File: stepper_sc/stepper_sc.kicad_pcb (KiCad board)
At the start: 2 copper layers, 90 x 120 mm, 24 parts, among them J1 PWR_24V, J10 BUZZ, J11 Black_Pill_front, J12 Black_Pill_back, J2 PUL, J3 DIR, J4 ES_L, J5 ES_R, J6 JOGL, J7 JOGR, J8 STEPL, J9 STEPR, Q1 BC547, Q2 BC547, U1 78M05

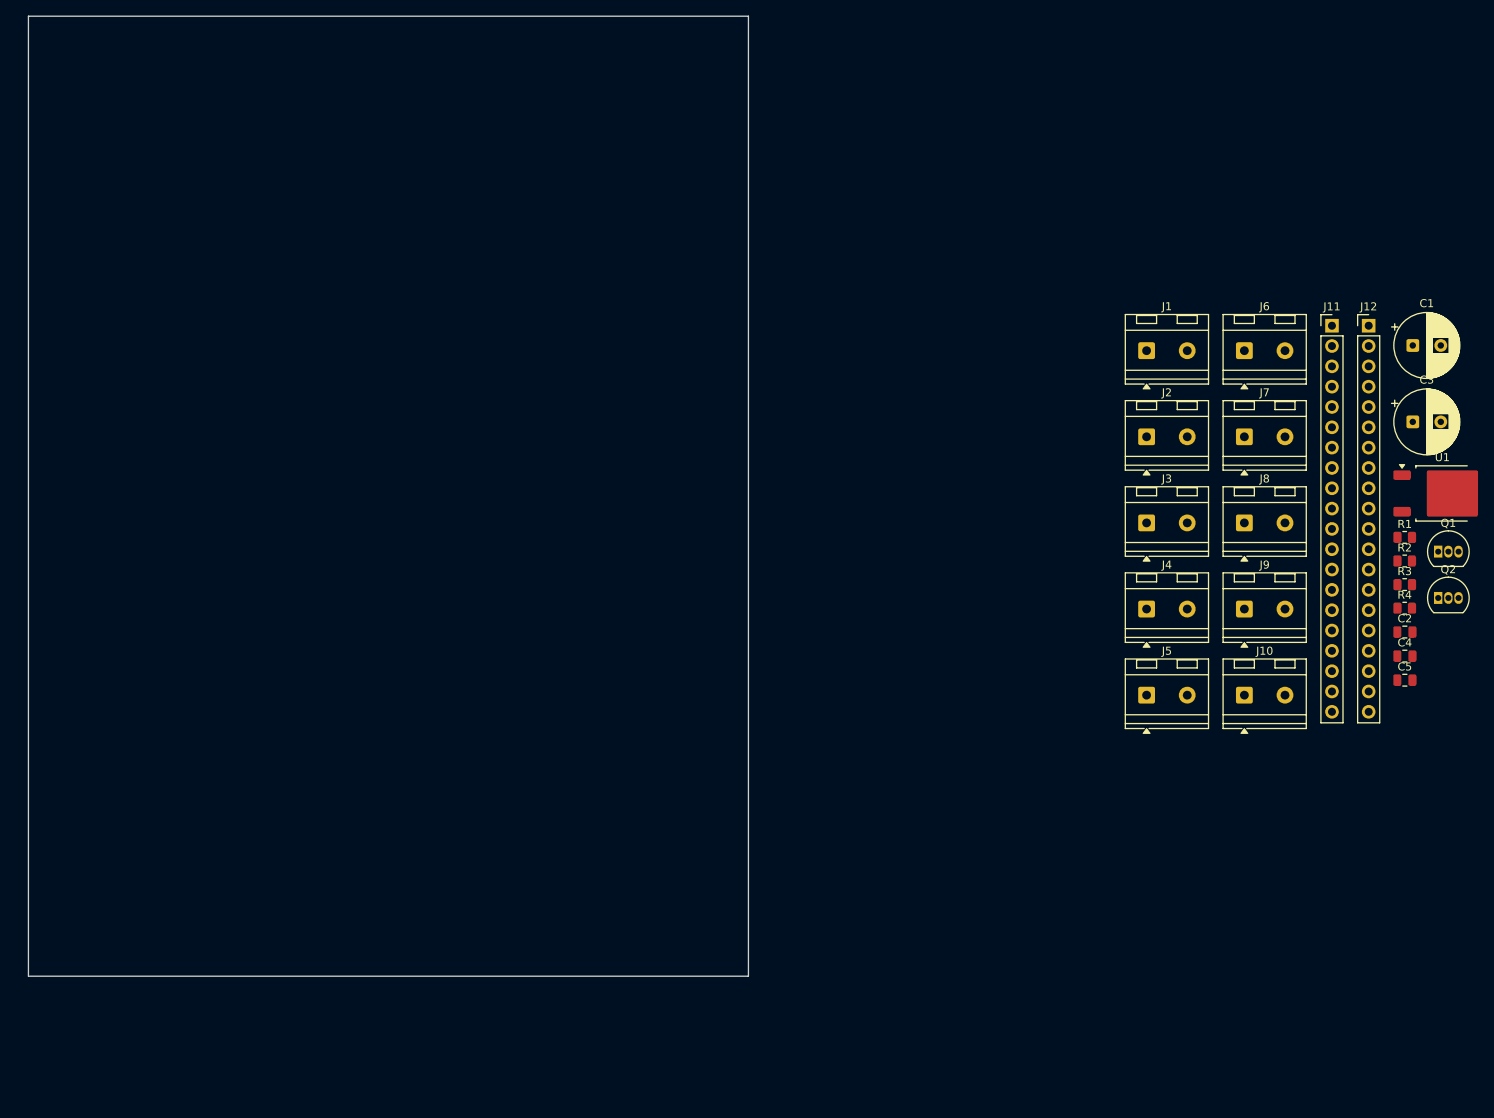
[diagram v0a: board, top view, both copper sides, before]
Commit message: Fix Q1/Q2 net assignments + orbit duplicate bug
- stepper_sc.kicad_pcb: assign correct nets to Q1 and Q2 pads
  BC547 TO-92_Inline pinout: pad1=C, pad2=B, pad3=E
  Q1: C→Net-(J2-Pin_2), B→Net-(Q1-PadB), E→GND
  Q2: C→Net-(J3-Pin_2), B→Net-(Q2-PadB), E→GND
  Root cause: KiCad couldn't map Q_NPN symbolic pins (B,C,E) to
  numeric pads (1,2,3) during Update PCB from Schematic.

- demo_orbit_all.py: fix duplicate footprint bug
  Use update_items(fp) without begin_commit/push_commit wrapper.
  Having both caused each fp to be sent twice → 1325 duplicates.

Co-Authored-By: Claude Sonnet 4.6 <noreply@anthropic.com>
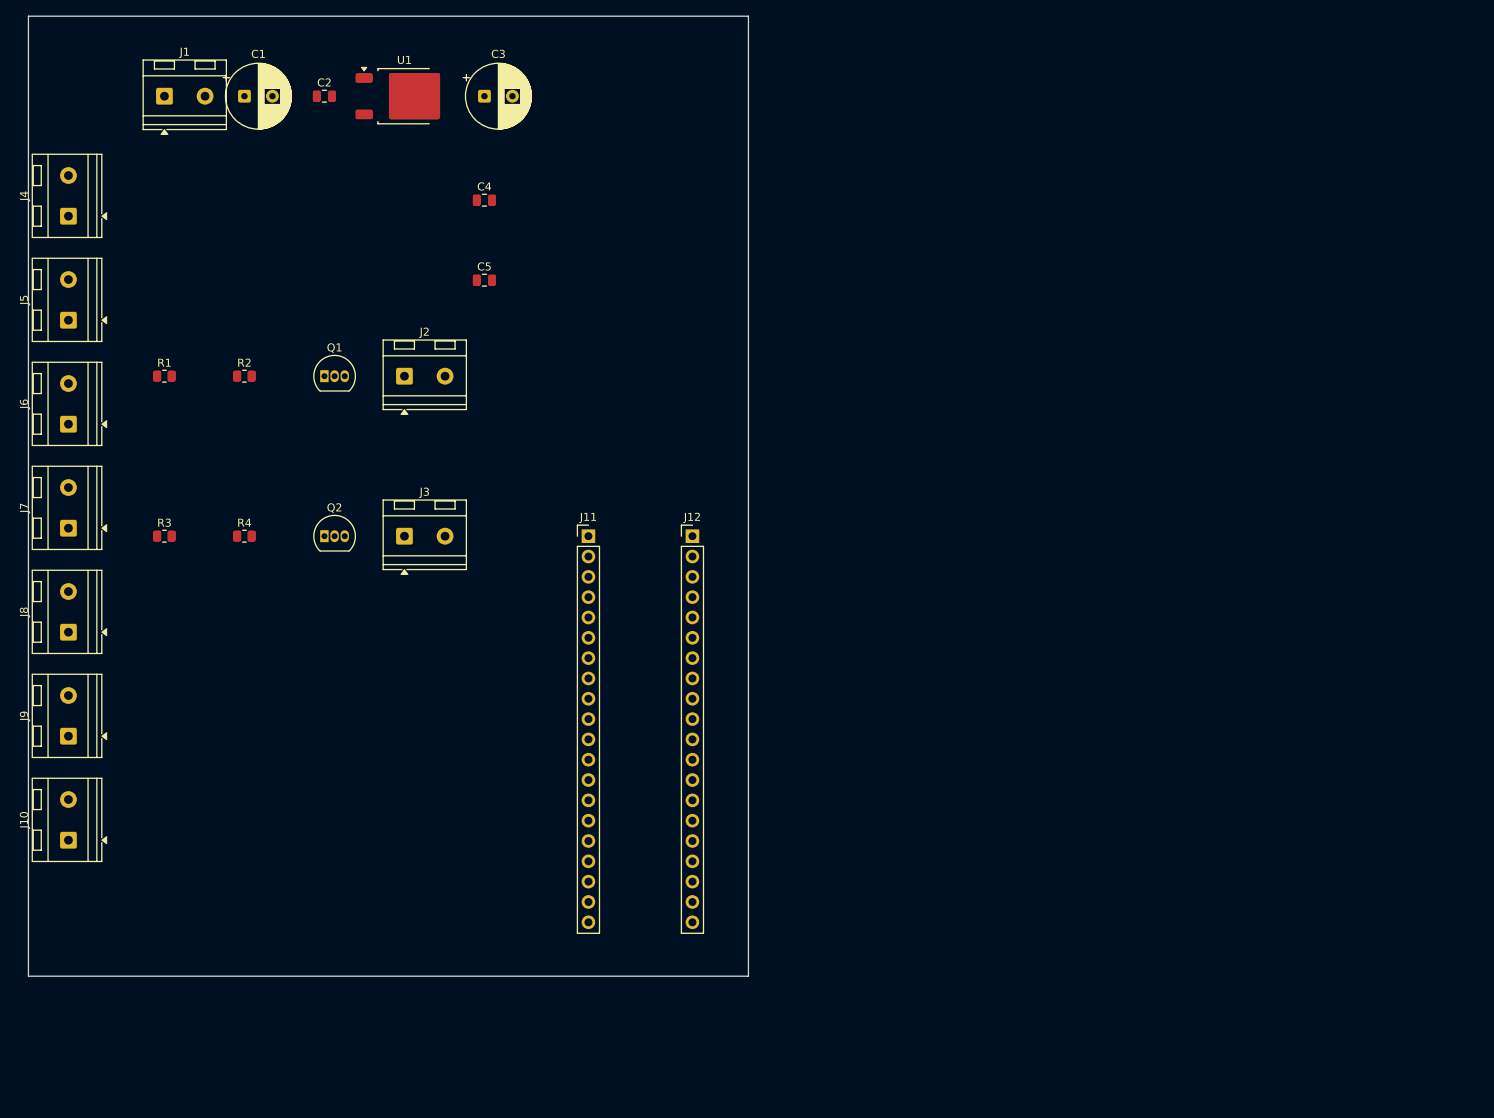
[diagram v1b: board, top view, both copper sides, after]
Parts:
- moved R1 156.3 mm to (42.0, 70.0)
- moved R3 155.1 mm to (42.0, 90.0)
- moved C2 150.7 mm to (62.0, 35.0)
- moved C1 149.3 mm to (52.0, 35.0)
- moved J10 148.1 mm to (30.0, 128.0), turned to 90 degrees
- moved J9 147.8 mm to (30.0, 115.0), turned to 90 degrees
- moved J8 147.6 mm to (30.0, 102.0), turned to 90 degrees
- moved J7 147.4 mm to (30.0, 89.0), turned to 90 degrees
- moved J6 147.3 mm to (30.0, 76.0), turned to 90 degrees
- moved R2 146.9 mm to (52.0, 70.0)
- moved R4 145.3 mm to (52.0, 90.0)
- moved J4 143.4 mm to (30.0, 50.0), turned to 90 degrees
- moved J5 142.7 mm to (30.0, 63.0), turned to 90 degrees
- moved Q1 140.9 mm to (62.0, 70.0)
- moved Q2 139.4 mm to (62.0, 90.0)
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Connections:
- Q1 pad 1: (no net) -> Net-(J2-Pin_2)
- Q1 pad 2: (no net) -> Net-(Q1-PadB)
- Q1 pad 3: (no net) -> GND
- Q2 pad 1: (no net) -> Net-(J3-Pin_2)
- Q2 pad 2: (no net) -> Net-(Q2-PadB)
- Q2 pad 3: (no net) -> GND

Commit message: PCB: swap C1/C3→CP_Elec_8x6.2 SMD, Q1/Q2→SOT-23 SMD; assign pad nets
- C1, C3: Capacitor_THT:CP_Radial_D8.0mm_P3.50mm → Capacitor_SMD:CP_Elec_8x6.2
- Q1, Q2: Package_TO_SOT_THT:TO-92_Inline → Package_TO_SOT_SMD:SOT-23
- Q1 pads: pad1(B)→Net-(Q1-PadB), pad2(E)→GND, pad3(C)→Net-(J2-Pin_2)
- Q2 pads: pad1(B)→Net-(Q2-PadB), pad2(E)→GND, pad3(C)→Net-(J3-Pin_2)
- Re-placed all 24 footprints after footprint swap

Co-Authored-By: Claude Sonnet 4.6 <noreply@anthropic.com>
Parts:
- C1, C3: footprint Capacitor_THT:CP_Radial_D8.0mm_P3.50mm -> Capacitor_SMD:CP_Elec_8x6.2
- Q1, Q2: footprint Package_TO_SOT_THT:TO-92_Inline -> Package_TO_SOT_SMD:SOT-23
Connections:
- Q1 pad 1: Net-(J2-Pin_2) -> Net-(Q1-PadB)
- Q1 pad 2: Net-(Q1-PadB) -> GND
- Q1 pad 3: GND -> Net-(J2-Pin_2)
- Q2 pad 1: Net-(J3-Pin_2) -> Net-(Q2-PadB)
- Q2 pad 2: Net-(Q2-PadB) -> GND
- Q2 pad 3: GND -> Net-(J3-Pin_2)

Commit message: PCB: reorganize terminal block column, extend board outline
- Move J1 above J4 in the left screw terminal column (rot=90°, 13mm spacing)
- Move J2, J3 into the same column below J10 (y=141, y=154, rot=90°)
- Extend edge cuts to fit full terminal column (J1→J2→J3→J4→...→J10)
- Board outline: x=25→115, y=25.26→160.66 (4.00mm gap above J1 and below J3 body)

Co-Authored-By: Claude Sonnet 4.6 <noreply@anthropic.com>
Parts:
- moved J2 82.5 mm to (30.0, 141.0), turned to 90 degrees
- moved J3 76.6 mm to (30.0, 154.0), turned to 90 degrees
- moved J1 12.2 mm to (30.0, 37.0), turned to 90 degrees
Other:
- board size 90 x 120 mm -> 90 x 135.4 mm

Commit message: PCB: layout power rail row — caps, regulator, equal spacing
- J1 placed in terminal column above J4, rot=90°, 13mm spacing
- J2, J3 moved into terminal column below J10 (y=141, y=154)
- Edge cuts extended and fine-tuned: 4.00mm gap above J1 and below J3 bodies
- C1 rotated +90° to match J1 polarity (+24V at bottom, GND at top)
- C2, C3, C4 rotated +90° to match polarity consistently
- C4 moved from (82,48) to power rail row at y=35
- U1 rotated 90° (3× -90°), center aligned to y=35
- Equal body spacing (4.13mm gaps) between C1–C2–U1–C3–C4

Co-Authored-By: Claude Sonnet 4.6 <noreply@anthropic.com>
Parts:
- moved C4 16.4 mm to (92.0, 35.0), turned to 90 degrees
- moved U1 1.71 mm to (70.3, 35.0), turned to 90 degrees
- moved C2 0.44 mm to (61.6, 35.0), turned to 90 degrees
- moved C3 0.44 mm to (82.4, 35.0), turned to 90 degrees
- turned C1 to 90 degrees

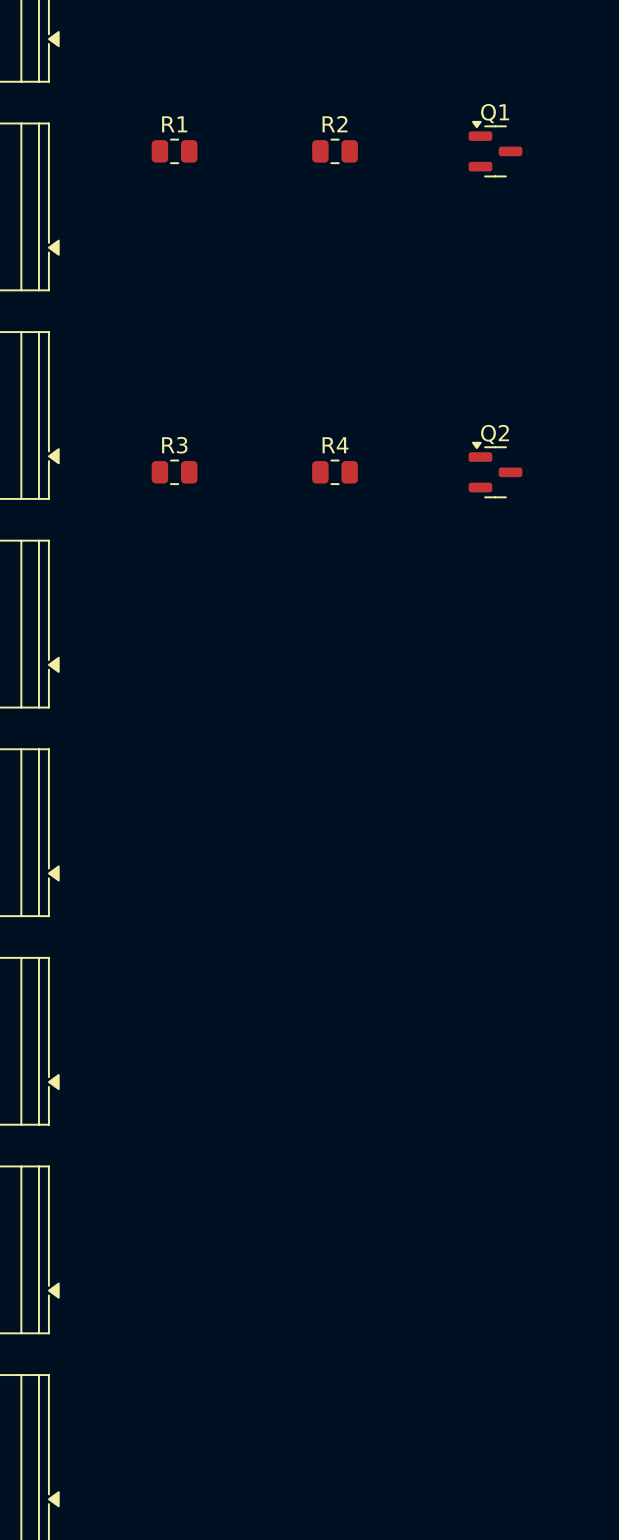
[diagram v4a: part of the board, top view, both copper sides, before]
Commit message: PCB: place NPN buffer groups Q1/Q2 aligned to screw terminals
- Q1 group (Q1 rot=0°, R2 rot=-90°, R1 rot=90°) at y=135.92
  Q1 pad3 (collector) aligned with J2 pad2 — direct horizontal trace
- Q2 group (Q2 rot=0°, R4 rot=-90°, R3 rot=90°) at y=148.92
  Q2 pad3 (collector) aligned with J3 pad2 — direct horizontal trace
- Both groups 2mm right of terminal block edge, equal body spacing

Co-Authored-By: Claude Sonnet 4.6 <noreply@anthropic.com>
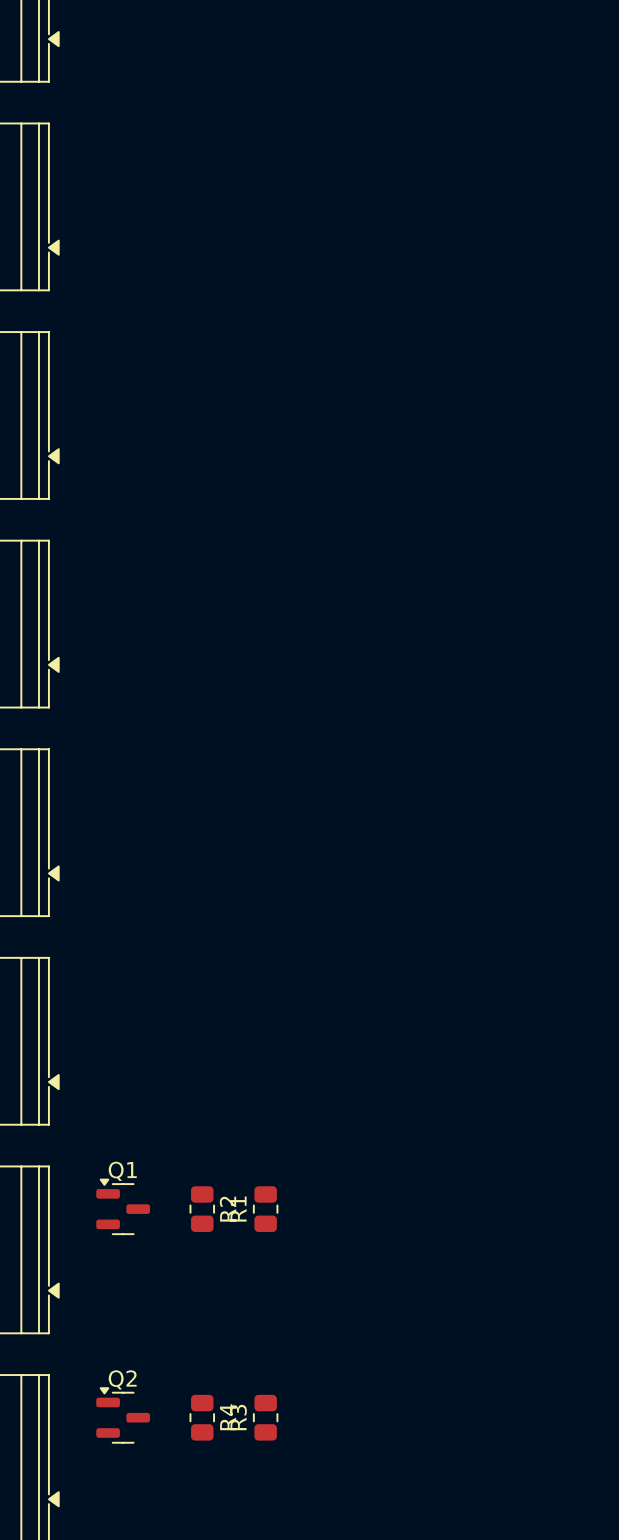
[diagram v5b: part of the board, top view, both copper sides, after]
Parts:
- moved Q1 69.9 mm to (38.8, 135.9)
- moved R2 66.4 mm to (43.7, 135.9), turned to -90 degrees
- moved R1 66.2 mm to (47.7, 135.9), turned to 90 degrees
- moved Q2 63.3 mm to (38.8, 148.9)
- moved R4 59.5 mm to (43.7, 148.9), turned to -90 degrees
- moved R3 59.2 mm to (47.7, 148.9), turned to 90 degrees

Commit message: PCB: align C5 +5V pad with J12 pin20, shift J11/J12/C5 group +10mm right
- C5 pad1 (+5V) x-aligned with J12 pin20 (+5V) at x=95.26mm
- J11/J12/C5 group shifted +10mm right (J11/J12 pin1 now at x=47)
- Add align_c5_j12.py helper script

Co-Authored-By: Claude Sonnet 4.6 <noreply@anthropic.com>
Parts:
- moved J12 72.9 mm to (47.0, 50.0), turned to 90 degrees
- moved J11 55.1 mm to (47.0, 63.0), turned to 90 degrees
- moved C5 12.4 mm to (94.3, 56.5), turned to 180 degrees

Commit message: PCB: add GND copper pour on F.Cu and B.Cu via IPC
- gnd_pour.py: creates filled Zone on both layers, net=GND
- Zone outline 0.5mm inset from Edge.Cuts (25.5,25.5)..(114.5,160.5)
- Zones refilled automatically after creation

Co-Authored-By: Claude Sonnet 4.6 <noreply@anthropic.com>
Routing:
- added copper zone on B.Cu, net GND
- added copper zone on F.Cu, net GND
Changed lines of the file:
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@@
 		(layer "Edge.Cuts")
+	)
+	(zone
+		(net 1)
+		(net_name "GND")
+		(layer "F.Cu")
+		(hatch edge 0.5)
+		(connect_pads
+			(clearance 0.3)
+		)
+		(min_thickness 0.25)
+		(filled_areas_thickness no)
+		(fill yes
+			(thermal_gap 0)
+			(thermal_bridge_width 0)
+		)
+		(polygon
+			(pts
+				(xy 25.5 25.5) (xy 114.5 25.5) (xy 114.5 160.5) (xy 25.5 160.5)
+			)
+		)
+	)
+	(zone
+		(net 1)
+		(net_name "GND")
+		(layer "B.Cu")
+		(hatch edge 0.5)
+		(connect_pads
+			(clearance 0.3)
+		)
+		(min_thickness 0.25)
+		(filled_areas_thickness no)
+		(fill yes
+			(thermal_gap 0)
+			(thermal_bridge_width 0)
+		)
+		(polygon
+			(pts
+				(xy 25.5 25.5) (xy 114.5 25.5) (xy 114.5 160.5) (xy 25.5 160.5)
+			)
+		)
 	)
 	(embedded_fonts no)

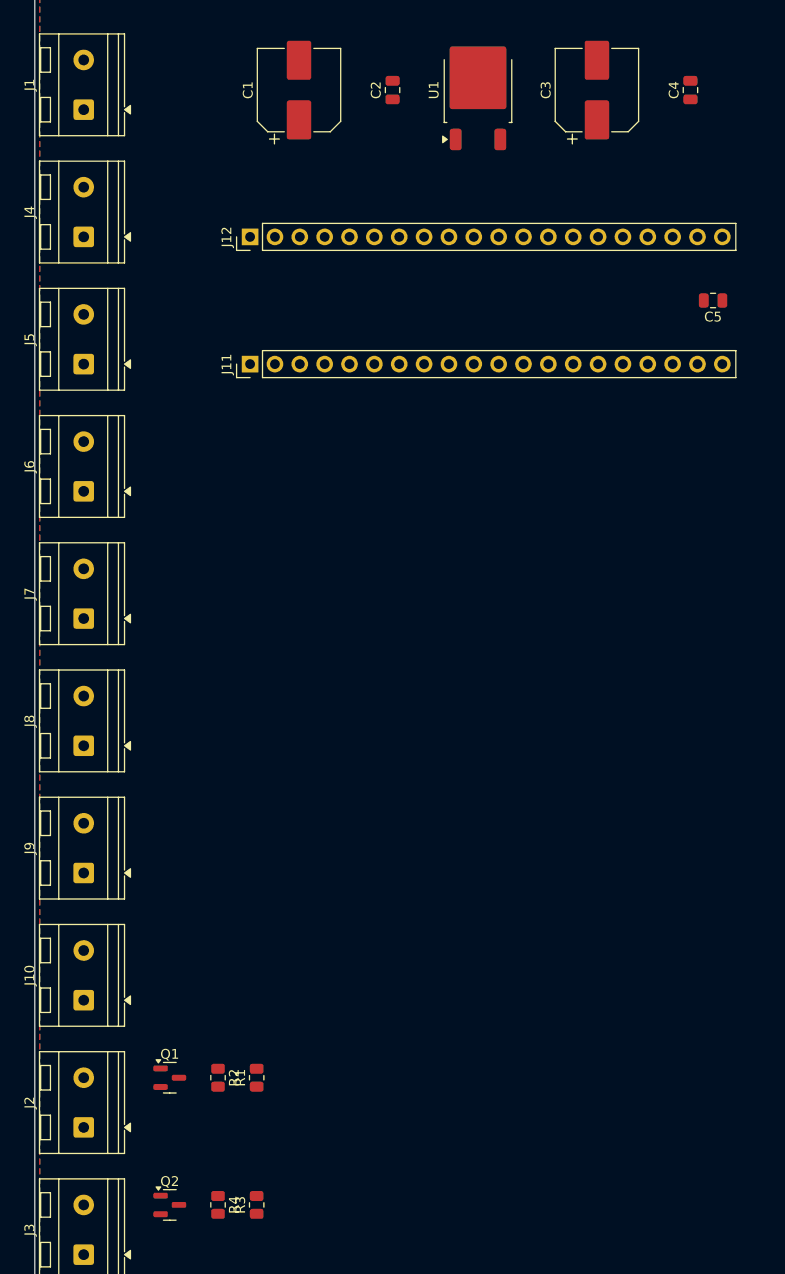
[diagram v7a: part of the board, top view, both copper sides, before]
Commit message: router: first homegrown A* PCB autorouter
- router/grid.py: two-layer obstacle grid (F.Cu + B.Cu), 0.1mm resolution
- router/astar.py: A* pathfinder, 8-directional + via transitions
- router/segments.py: convert A* path to 45° track segments
- router/router.py: main entry point, queries KiCad IPC, routes all unconnected nets

First run: 9 nets routed, 124 tracks + 4 vias, 0 failures.
No crossings — per-net pad exclusion prevents short circuits.

Co-Authored-By: Claude Sonnet 4.6 <noreply@anthropic.com>
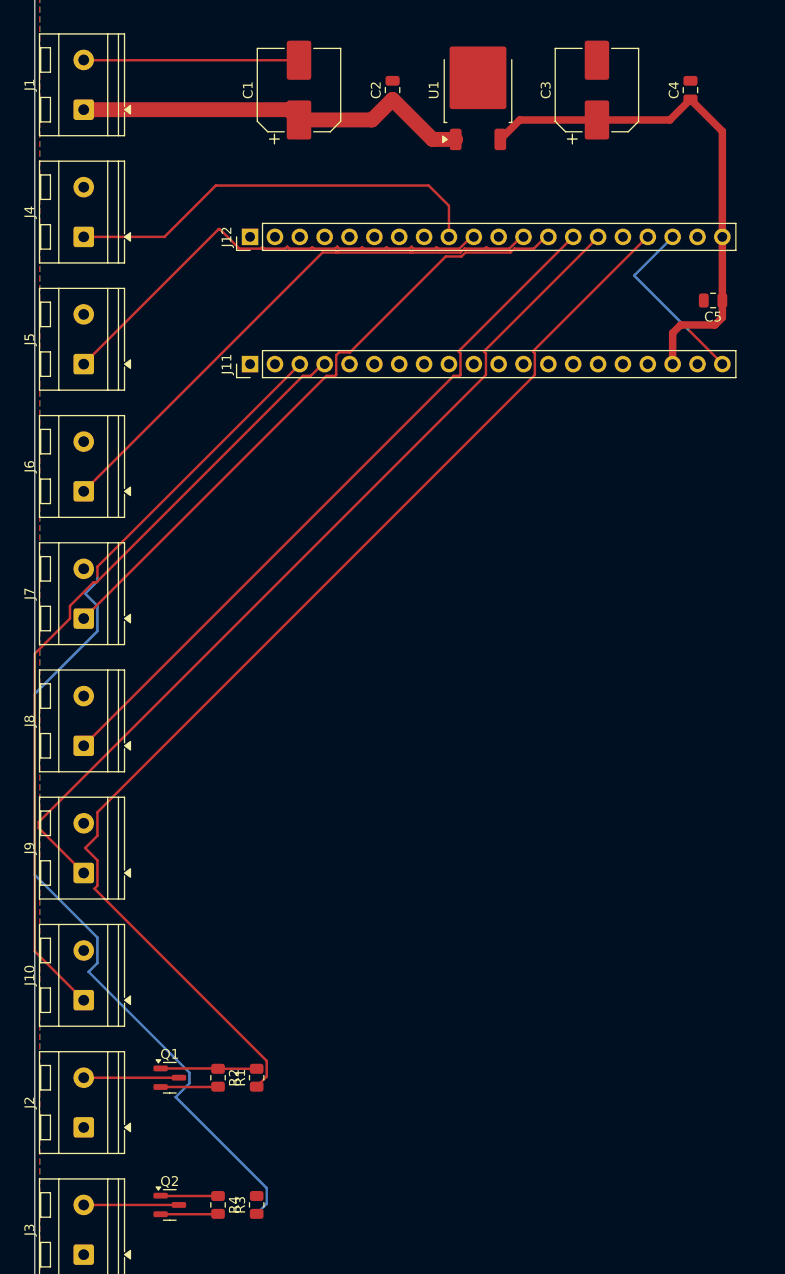
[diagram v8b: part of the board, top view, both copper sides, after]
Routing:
- net Net-(J12-Pin_17): track 0.00 -> 119.1 mm
- net Net-(J11-Pin_3): track 0.00 -> 111.2 mm, vias 0 -> 2
- net Net-(J12-Pin_15): track 0.00 -> 90.8 mm
- net Net-(J10-Pin_1): track 0.00 -> 80.2 mm
- net Net-(J12-Pin_14): track 0.00 -> 73.2 mm
- net Net-(J12-Pin_13): track 0.00 -> 64.9 mm
- net Net-(J12-Pin_12): track 0.00 -> 56.0 mm
- net +5V: track 0.00 -> 53.7 mm
- net Net-(J12-Pin_10): track 0.00 -> 47.9 mm
- net Net-(J12-Pin_9): track 0.00 -> 43.5 mm
- net +24V: track 0.00 -> 41.0 mm
- net GND: track 0.00 -> 33.8 mm
- net +3.3V: track 0.00 -> 18.3 mm, vias 0 -> 2
- net Net-(Q1-PadB): track 0.00 -> 9.83 mm
- net Net-(J3-Pin_2): track 0.00 -> 9.73 mm
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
